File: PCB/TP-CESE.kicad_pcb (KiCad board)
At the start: 2 copper layers, 87 x 61 mm, 43 parts, among them J1 Screw_Terminal_01x04, J3 Screw_Terminal_01x02, J4 Conn_01x05_Male, J5 test, Q1 IRF540N, Q2 IRF540N, Q3 IRF540N, Q4 IRF540N, U1 4N25, U2 4N25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

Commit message: Gerbers, Bom ,mejoro conexiones
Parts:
- added FID1: Fiducial, Fiducial:Fiducial_1mm_Mask2mm, F.Cu at (99.0, 69.0)
- added FID2: Fiducial, Fiducial:Fiducial_1mm_Mask2mm, F.Cu at (161.0, 70.0)
- added FID3: Fiducial, Fiducial:Fiducial_1mm_Mask2mm, F.Cu at (158.0, 114.0)
- moved R17 2.00 mm to (157.0, 99.0)
- moved R18 2.00 mm to (154.0, 99.0)
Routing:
- net +3V3: track 44.9 -> 47.2 mm
- net Net-(R17-Pad1): track 11.5 -> 13.5 mm
- net Net-(R18-Pad2): track 22.5 -> 24.1 mm
- net +5VP: track 89.3 -> 90.7 mm
- net GND: track 66.5 -> 67.3 mm
- net Net-(U3-Pad1): track 35.3 -> 36.0 mm
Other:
- net class Default: clearance 0.8 -> 0.22
- rule trace_clearance: 0.8 -> 0.22
- board text added: "+VCC"
- board text added: "Driver motor PaP-Ads1015"
- board text added: "GND"
- board text added: "Ind. Argentina -2020"

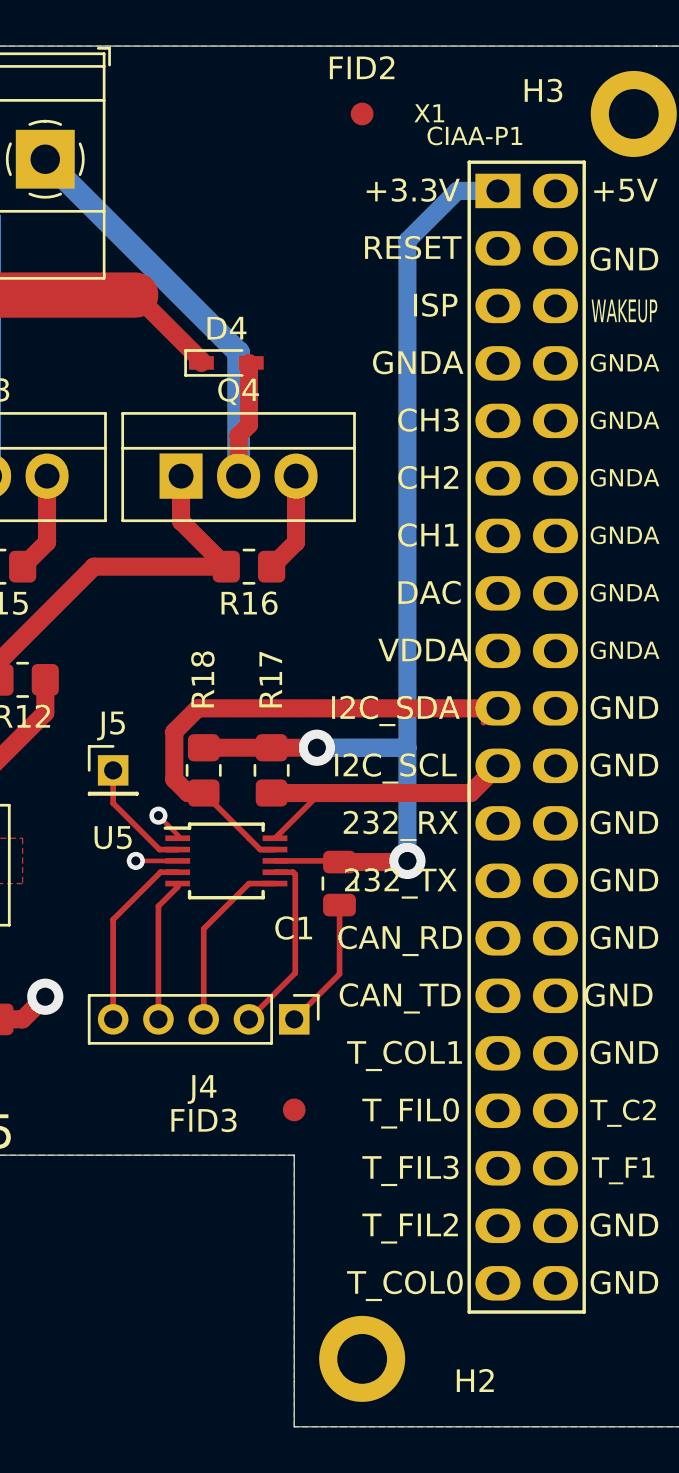
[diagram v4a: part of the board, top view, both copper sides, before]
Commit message: Carpeta Shapes3D
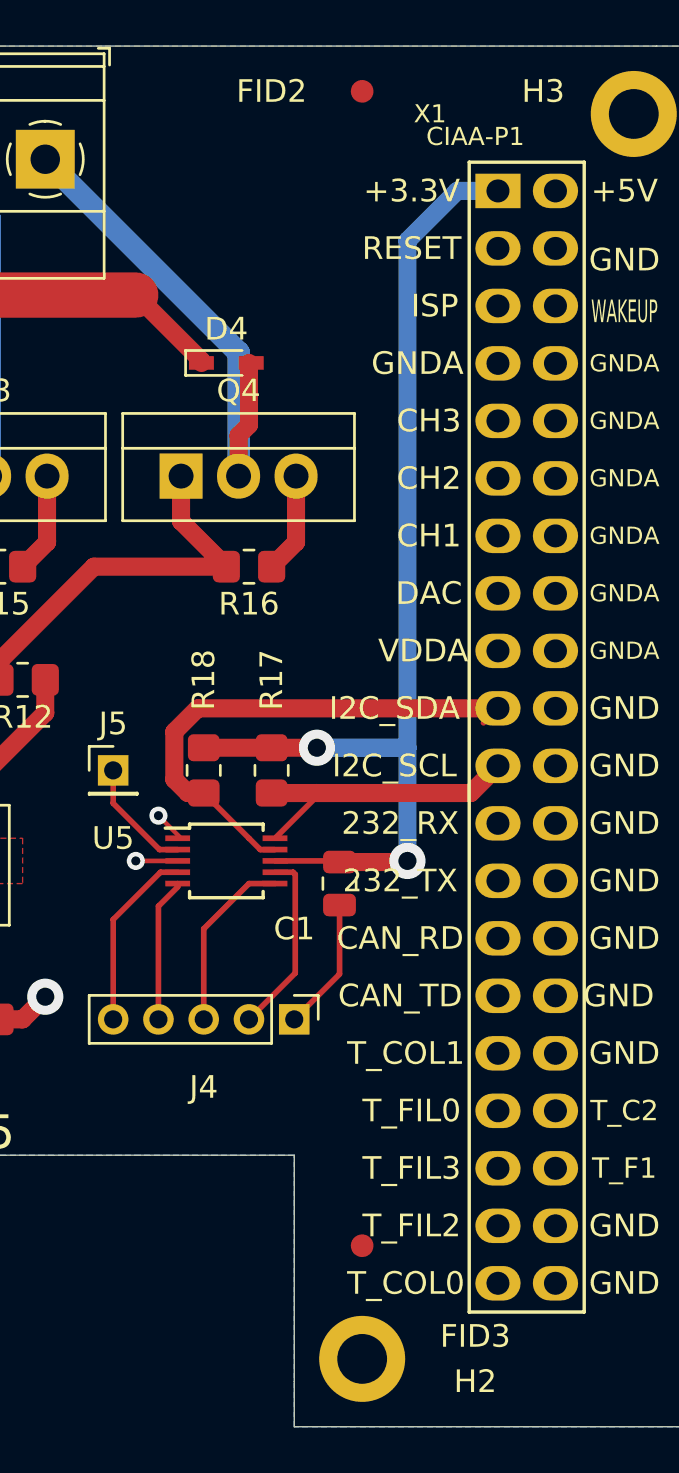
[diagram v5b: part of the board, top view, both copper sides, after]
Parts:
- moved FID3 6.71 mm to (161.0, 120.0)
- moved FID2 1.00 mm to (161.0, 69.0)
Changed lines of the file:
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@@
   (general
     (thickness 1.6)
-    (drawings 22)
+    (drawings 23)
     (tracks 211)
     (zones 0)
@@
     (38 B.Mask user)
     (39 F.Mask user)
-    (40 Dwgs.User user hide)
+    (40 Dwgs.User user)
     (41 Cmts.User user)
     (42 Eco1.User user)
@@
   )
   (module Fiducial:Fiducial_1mm_Mask2mm (layer F.Cu)
-    (at 158 114)
+    (at 161 120)
     (descr "Circular Fiducial, 1mm bare copper, 2mm soldermask opening (Level A)")
     (tags fiducial)
     (attr smd)
-    (fp_text reference FID3 (at -4 0.5) (layer F.SilkS)
+    (fp_text reference FID3 (at 5 4) (layer F.SilkS)
       (effects (font (size 1 1) (thickness 0.15)))
     )
@@
   )
   (module Fiducial:Fiducial_1mm_Mask2mm (layer F.Cu)
-    (at 161 70)
+    (at 161 69)
     (descr "Circular Fiducial, 1mm bare copper, 2mm soldermask opening (Level A)")
     (tags fiducial)
     (attr smd)
-    (fp_text reference FID2 (at 0 -2) (layer F.SilkS)
+    (fp_text reference FID2 (at -4 0) (layer F.SilkS)
       (effects (font (size 1 1) (thickness 0.15)))
     )
@@
     )
   )
+  (dimension 2 (width 0.15) (layer Dwgs.User)
+    (gr_text "2,000 mm" (at 129 112.3) (layer Dwgs.User)
+      (effects (font (size 1 1) (thickness 0.15)))
+    )
+    (feature1 (pts (xy 130 108) (xy 130 111.586421)))
+    (feature2 (pts (xy 128 108) (xy 128 111.586421)))
+    (crossbar (pts (xy 128 111) (xy 130 111)))
+    (arrow1a (pts (xy 130 111) (xy 128.873496 111.586421)))
+    (arrow1b (pts (xy 130 111) (xy 128.873496 110.413579)))
+    (arrow2a (pts (xy 128 111) (xy 129.126504 111.586421)))
+    (arrow2b (pts (xy 128 111) (xy 129.126504 110.413579)))
+  )
   (gr_text "Ind. Argentina -2020" (at 148 114) (layer B.SilkS)

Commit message: Correcciones Realizadas
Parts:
- D1, D2, D3, D4: footprint Diode_SMD:D_SC-80_HandSoldering -> Diode_THT:D_DO-35_SOD27_P7.62mm_Horizontal
- moved FID2 7.91 mm to (168.5, 66.5)
- moved FID3 6.71 mm to (158.0, 114.0)
- moved D1 4.00 mm to (119.0, 81.0)
- moved FID1 3.91 mm to (96.0, 66.5)
- moved D2 3.00 mm to (130.0, 81.0)
- moved D4 3.00 mm to (152.0, 81.0)
- moved H1 2.55 mm to (91.5, 67.5)
- moved H3 2.50 mm to (173.0, 67.5)
- moved R12 2.24 mm to (144.0, 94.0), turned to 0 degrees
- moved D3 2.00 mm to (141.0, 81.0)
- moved J5 2.00 mm to (148.0, 99.0)
- moved J1 1.50 mm to (147.0, 73.5)
- turned R10 to 0 degrees
- turned R11 to 0 degrees
- turned R9 to 0 degrees
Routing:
- net Net-(D1-Pad2): track 23.5 -> 18.6 mm
- net +5VP: track 90.7 -> 94.6 mm
- net Net-(D2-Pad2): track 20.6 -> 18.0 mm
- net Net-(D3-Pad2): track 20.3 -> 17.7 mm
- net Net-(Q3-Pad1): track 18.0 -> 15.5 mm
- net Net-(J5-Pad1): track 5.15 -> 7.41 mm
- net Net-(Q2-Pad1): track 17.0 -> 15.1 mm
- net Net-(J4-Pad4): track 6.35 -> 8.26 mm
- net GND: track 67.3 -> 65.4 mm, vias 7 -> 8
- net Net-(R17-Pad1): track 13.5 -> 15.2 mm
- net Net-(J4-Pad5): track 8.13 -> 9.10 mm
- net Net-(Q4-Pad1): track 17.4 -> 16.5 mm
- net Net-(R18-Pad2): track 24.1 -> 25.0 mm
- net Net-(Q1-Pad1): track 16.0 -> 15.2 mm
- net Net-(D4-Pad2): track 22.9 -> 22.2 mm
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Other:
- board size 87 x 61 mm -> 87 x 63 mm
- net class Default: clearance 0.22 -> 0.25
- net class U5 removed
- rule trace_clearance: 0.22 -> 0.25
- board text added: "Driver motor PaP-Ads1015 -Ver 1.0"
- board text added: "Ind Agentina V 1.0 -10/2020"
- board text added: "L1"
- board text added: "L2"
- board text added: "L3"
- board text added: "L4"
- board text added: "Minimos (Mayers 10 Mils): Grillas : 1mm, 0,5mm Via: 1,6 mm / 1 mm Margen :0,25 mm Pista : 1,5mm/0,8mm/0,25 mm Dist a Borde: 0,3 mm Terminacion :Cu+Flux Espesor placa:1,6mm Espesor del Cobre:Estandar (35um/1Oz) Material :FR4"
- board text removed: "Driver motor PaP-Ads1015"
- board text removed: "Ind. Argentina -2020"

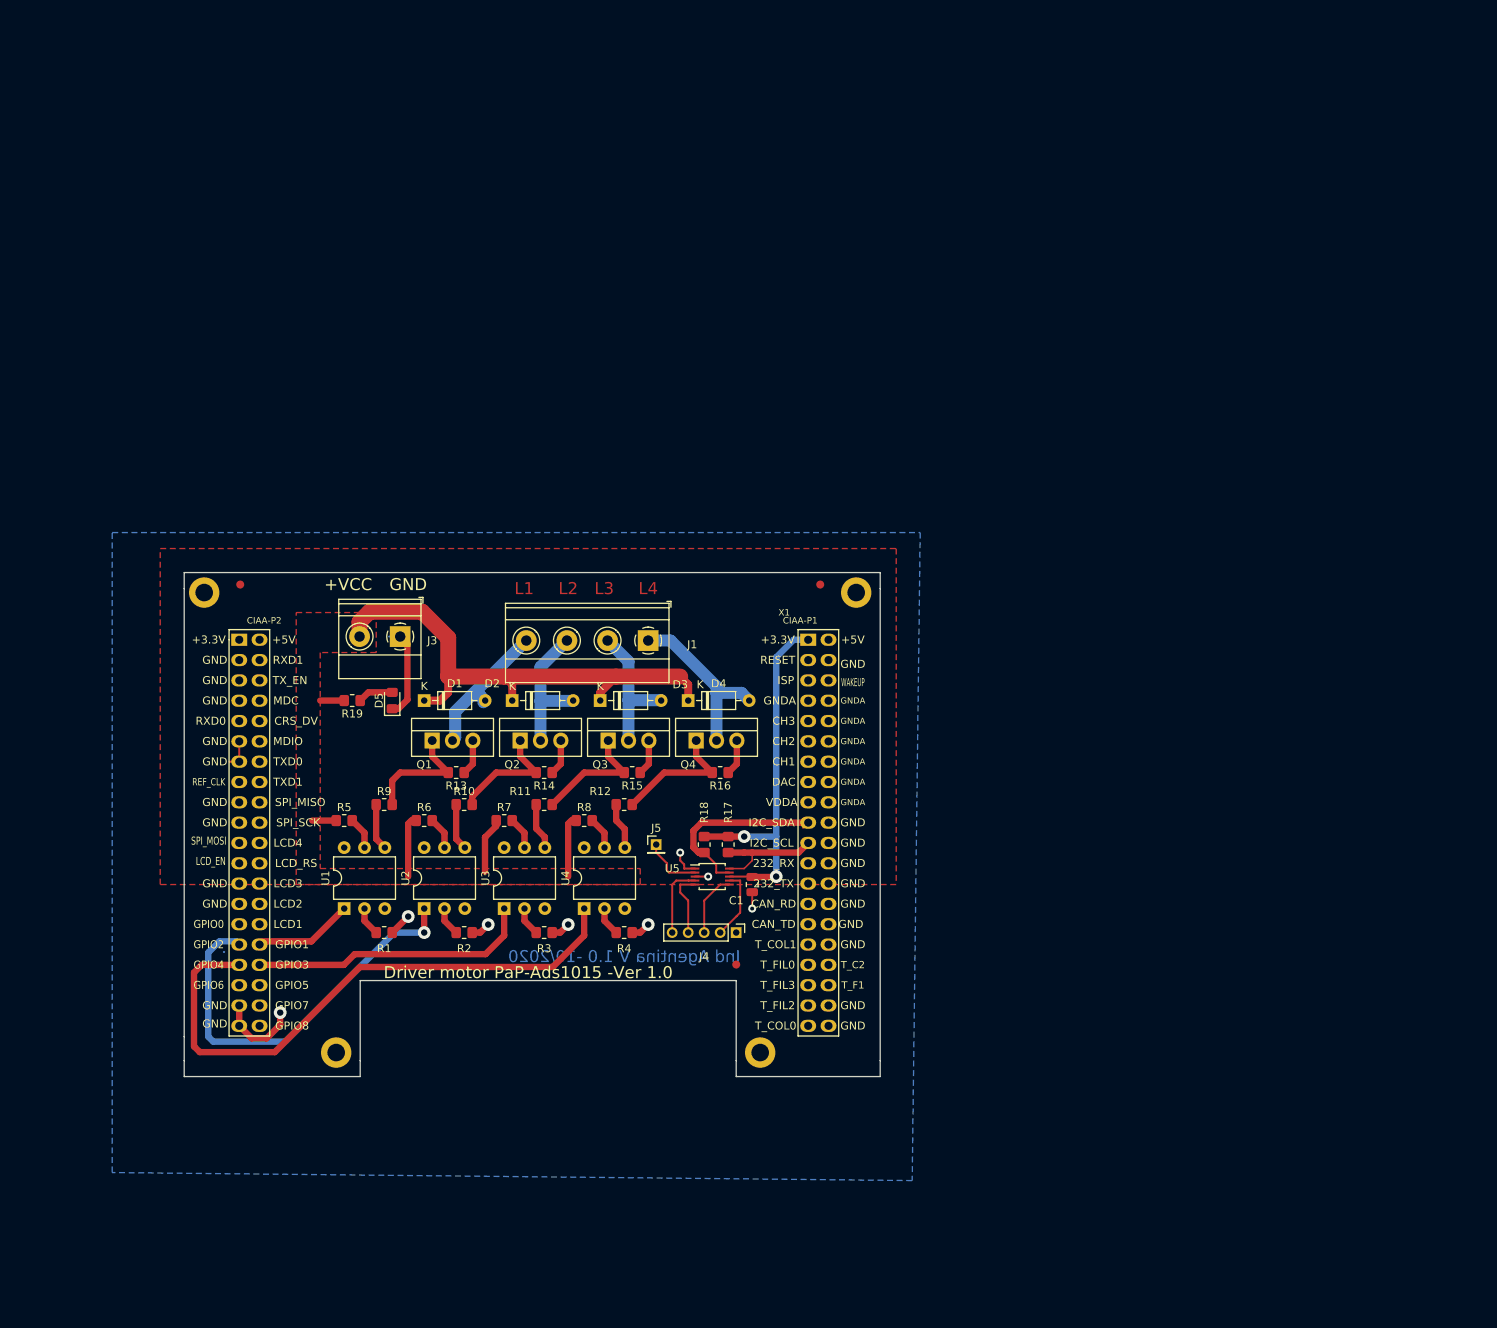
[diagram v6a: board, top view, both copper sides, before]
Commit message: Se agrga integrado L297 , para manejo de motor paso a paso, se sacan los optoacopladores ya que el L297 maneja directamente los Irf
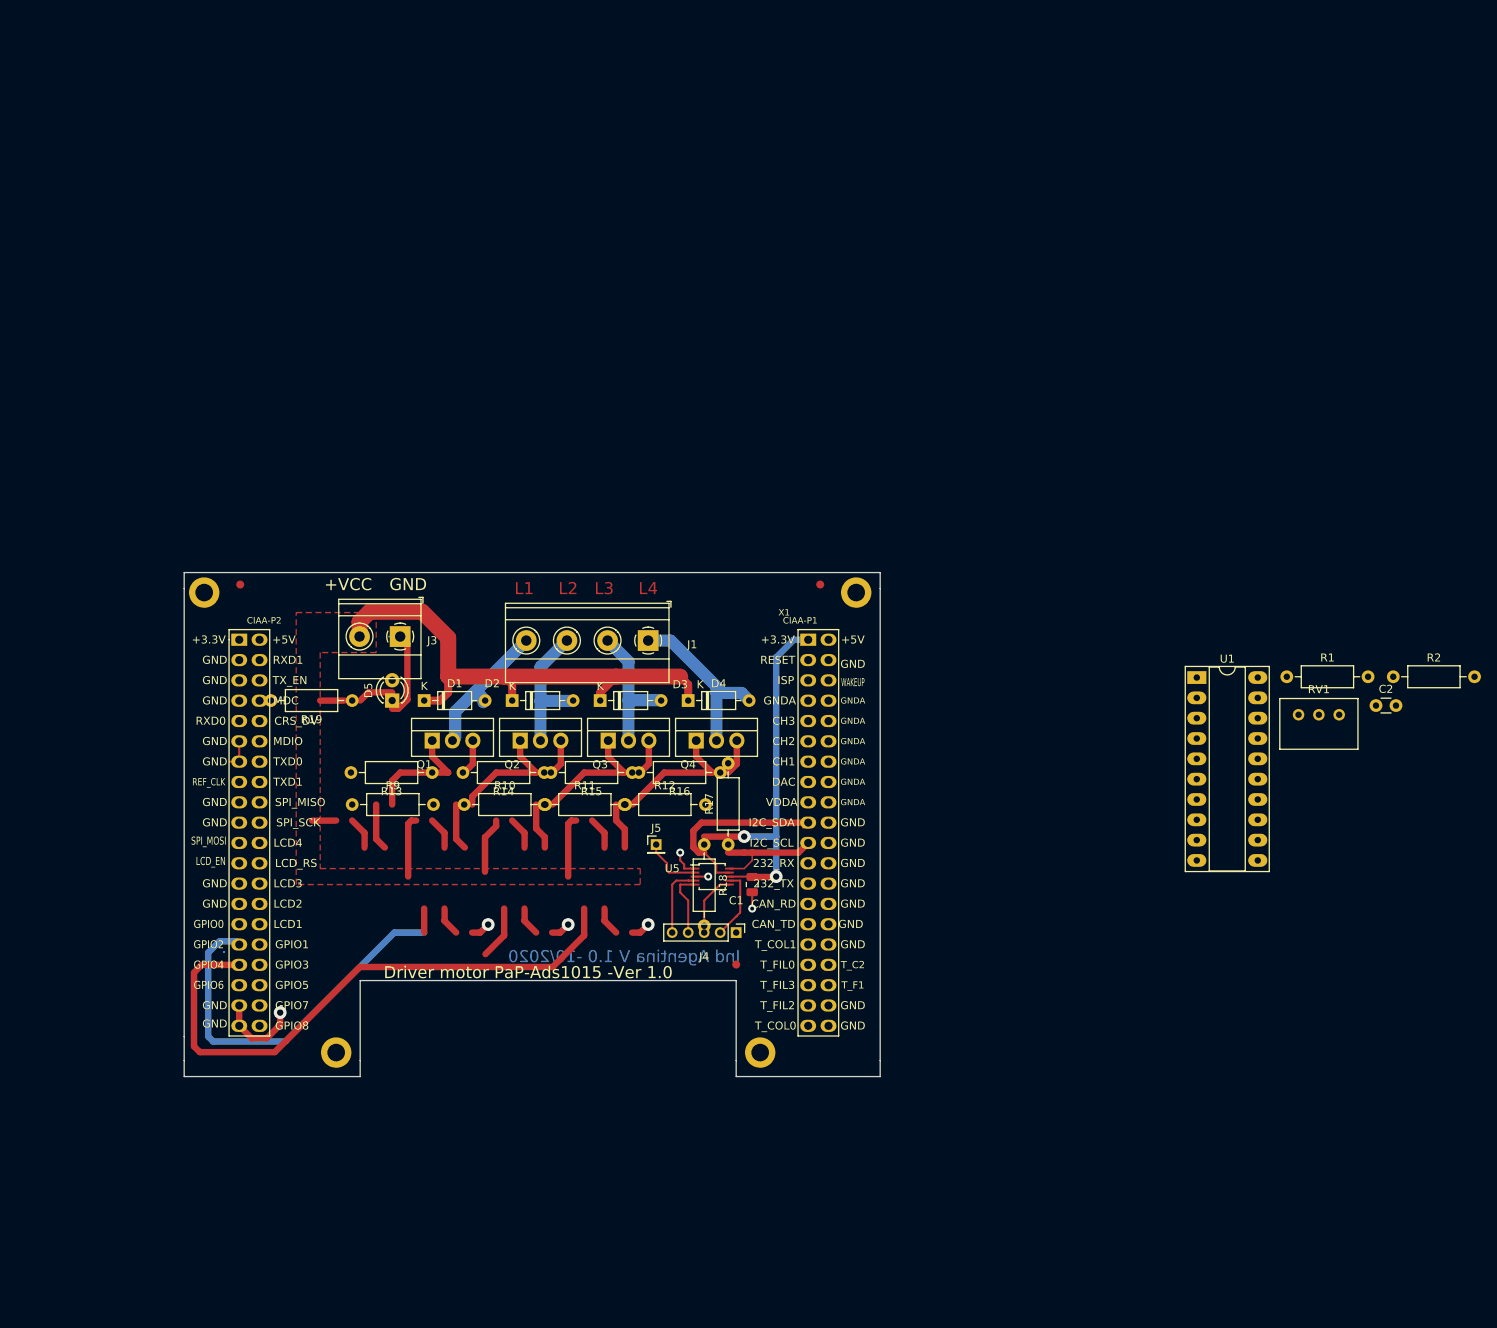
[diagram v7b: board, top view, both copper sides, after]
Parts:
- removed R3, R4: 180, Resistor_SMD:R_0805_2012Metric_Pad1.20x1.40mm_HandSolder
- removed R5, R6, R7, R8: 100, Resistor_SMD:R_0805_2012Metric_Pad1.20x1.40mm_HandSolder
- removed U2, U3, U4: 4N25, Package_DIP:DIP-6_W7.62mm
- added C2: C, Capacitor_THT:C_Disc_D3.0mm_W1.6mm_P2.50mm, F.Cu at (238.0, 81.6)
- added RV1: 1K, Potentiometer_THT:Potentiometer_Bourns_3299W_Vertical, F.Cu at (233.4, 82.8)
- D5: footprint LED_SMD:LED_0805_2012Metric_Pad1.15x1.40mm_HandSolder -> LED_THT:LED_D3.0mm_Clear
- R1: value 180 -> 22K; footprint Resistor_SMD:R_0805_2012Metric_Pad1.20x1.40mm_HandSolder -> Resistor_THT:R_Axial_DIN0207_L6.3mm_D2.5mm_P10.16mm_Horizontal
- R10, R11, R12, R13, R14, R15, R16, R17, R18, R19, R9: footprint Resistor_SMD:R_0805_2012Metric_Pad1.20x1.40mm_HandSolder -> Resistor_THT:R_Axial_DIN0207_L6.3mm_D2.5mm_P10.16mm_Horizontal
- R2: value 180 -> 1K; footprint Resistor_SMD:R_0805_2012Metric_Pad1.20x1.40mm_HandSolder -> Resistor_THT:R_Axial_DIN0207_L6.3mm_D2.5mm_P10.16mm_Horizontal
- U1: value 4N25 -> L297; footprint Package_DIP:DIP-6_W7.62mm -> Package_DIP:DIP-20_W7.62mm_Socket_LongPads
- moved R2 120.5 mm to (240.1, 78.0)
- moved R1 117.3 mm to (226.8, 78.0)
- moved U1 110.4 mm to (215.6, 78.1), turned to 0 degrees
- moved R9 4.00 mm to (110.0, 94.0)
- moved R13 3.00 mm to (120.0, 90.0)
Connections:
- R1 pad 1: Net-(R1-Pad1) -> +5VP
- R1 pad 2: GND -> Net-(C2-Pad1)
- R2 pad 2: GND -> +5VP
- U1 pad 2: Net-(R1-Pad1) -> GND
- U1 pad 6: Net-(U1-Pad6) -> Net-(R10-Pad1)
- X1 pad 71: Net-(U2-Pad1) -> Net-(U1-Pad19)
- X1 pad 72: Net-(U1-Pad1) -> Net-(U1-Pad20)
- X1 pad 73: Net-(U4-Pad1) -> Net-(U1-Pad10)
- X1 pad 74: Net-(U3-Pad1) -> Net-(U1-Pad18)
- X1 pad 76: Net-(X1-Pad76) -> Net-(U1-Pad17)
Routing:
- net Net-(U4-Pad1): track 73.8 -> 0.00 mm
- net Net-(U1-Pad10): track 0.00 -> 73.8 mm
- net Net-(U2-Pad1): track 51.6 -> 0.00 mm, vias 1 -> 0
- net Net-(U1-Pad19): track 0.00 -> 51.6 mm
- net Net-(U3-Pad1): track 36.0 -> 0.00 mm
- net Net-(U1-Pad1): track 12.3 -> 0.00 mm
- net Net-(U1-Pad18): track 0.00 -> 7.22 mm
- net Net-(U1-Pad5): track 4.02 -> 0.00 mm
- net Net-(R5-Pad2): track 0.00 -> 4.02 mm
- net Net-(R1-Pad1): track 3.60 -> 0.00 mm
- net GND: track 65.4 -> 62.6 mm, vias 8 -> 7
- removed copper zone on B.Cu, net GND
